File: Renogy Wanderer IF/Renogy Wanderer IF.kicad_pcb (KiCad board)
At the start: 2 copper layers, 50.8 x 40.6 mm, 4 parts, among them J1 Conn_01x04, U1 WeMos_D1_mini

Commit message: Initial PCB design
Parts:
- removed A1: MINI-360, Module:MINI-360
- moved J1 28.3 mm to (99.1, 91.0), turned to 90 degrees
- moved U1 21.6 mm to (103.4, 52.1)
- moved A2 18.0 mm to (114.3, 86.4), turned to 180 degrees
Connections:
- J1 pad 1: +15V -> GND
- J1 pad 4: GND -> unconnected-(J1-Pad4)
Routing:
- net GND: track 0.00 -> 63.8 mm
- net +3V3: track 0.00 -> 38.1 mm
- net Net-(U1-Pad16): track 0.00 -> 34.1 mm, vias 0 -> 1
- net Net-(U1-Pad15): track 0.00 -> 28.4 mm, vias 0 -> 1
- net Net-(J1-Pad3): track 0.00 -> 11.2 mm, vias 0 -> 1
- net Net-(J1-Pad2): track 0.00 -> 10.8 mm, vias 0 -> 1
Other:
- board size 50.8 x 40.6 mm -> 35.6 x 50.8 mm
- board text added: "USB"

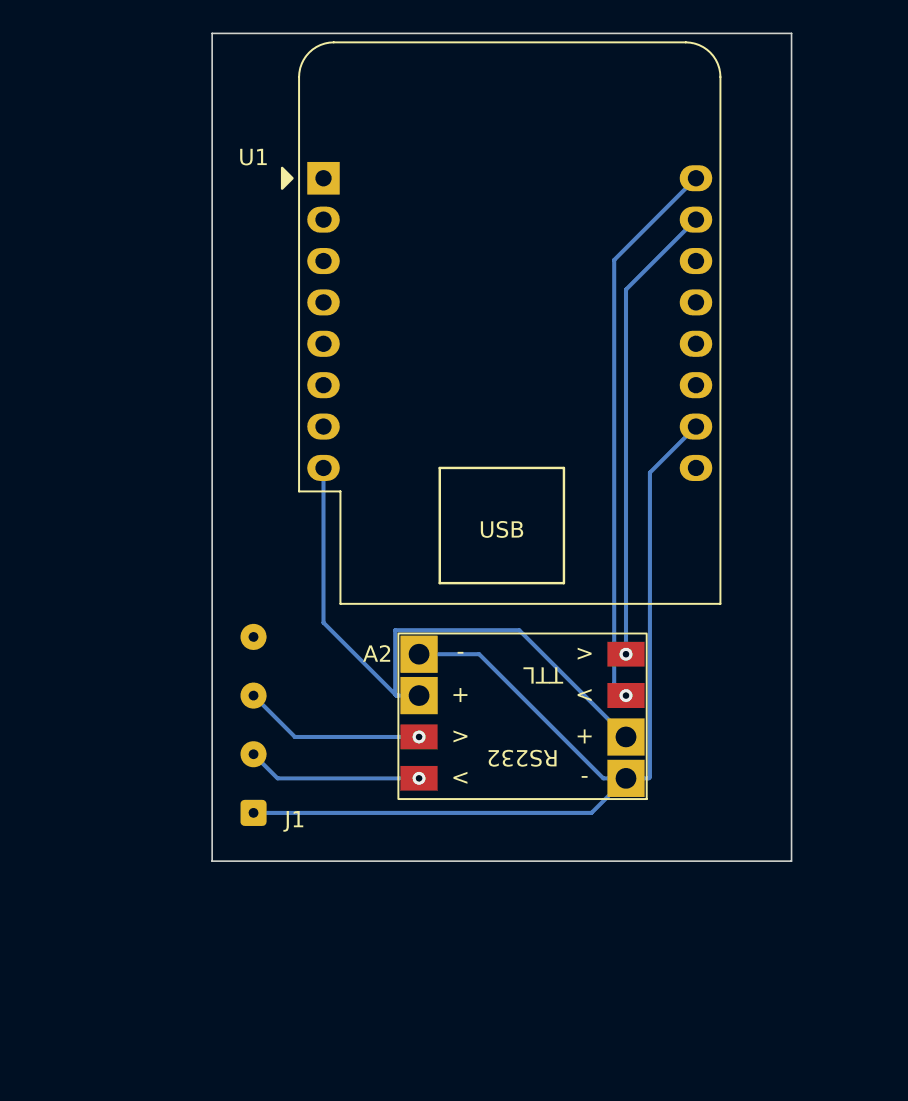
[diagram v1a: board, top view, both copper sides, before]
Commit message: Add wake from sleep
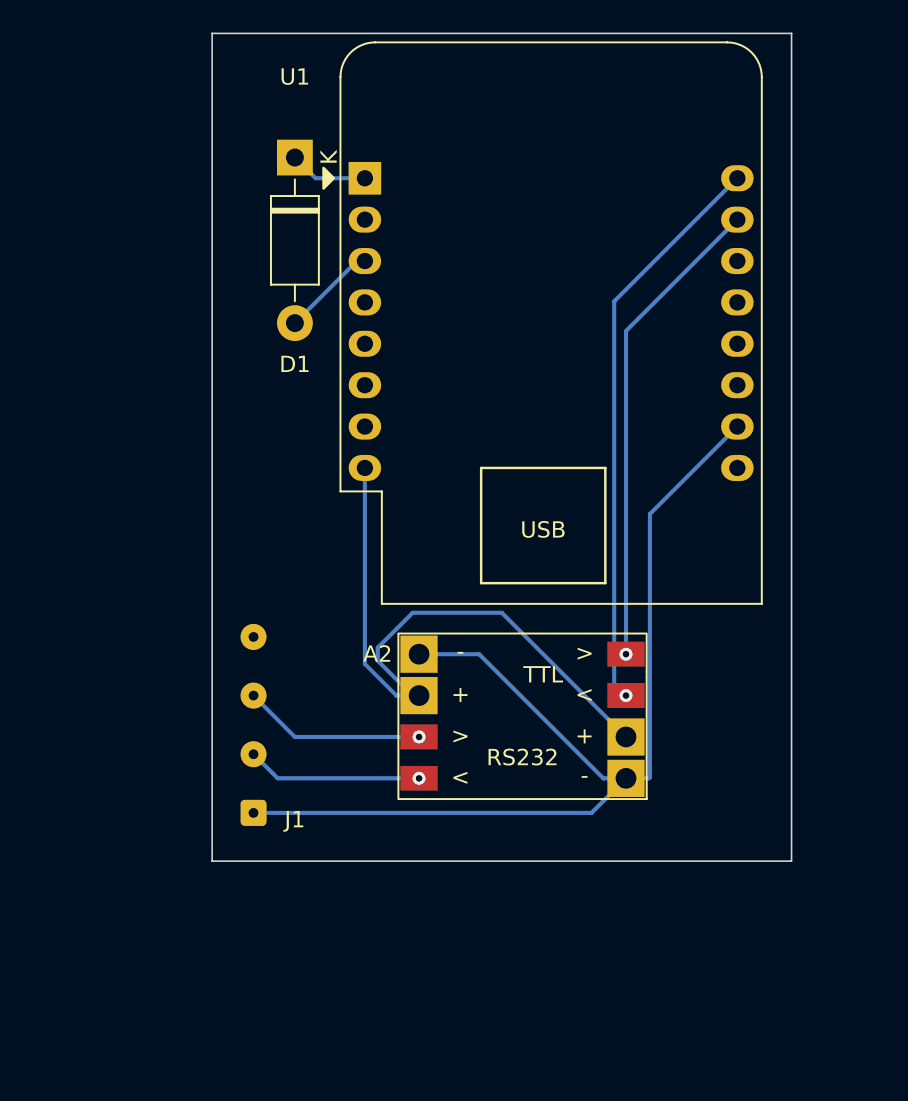
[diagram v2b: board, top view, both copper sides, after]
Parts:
- added D1: D_Schottky, Diode_THT:D_DO-41_SOD81_P10.16mm_Horizontal, F.Cu at (101.6, 50.8)
- moved U1 2.54 mm to (105.9, 52.1)
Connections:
- U1 pad 1: unconnected-(U1-Pad1) -> Net-(U1-Pad1)
- U1 pad 3: unconnected-(U1-Pad3) -> Net-(U1-Pad3)
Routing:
- net Net-(U1-Pad3): track 0.00 -> 5.87 mm
- net Net-(U1-Pad1): track 0.00 -> 4.82 mm
- net +3V3: track 38.1 -> 39.7 mm
- net GND: track 63.8 -> 64.8 mm
- net Net-(A2-Pad12): track 28.4 -> 29.5 mm
- net Net-(A2-Pad11): track 34.1 -> 35.2 mm

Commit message: Invert the RS232 module for easier mounting
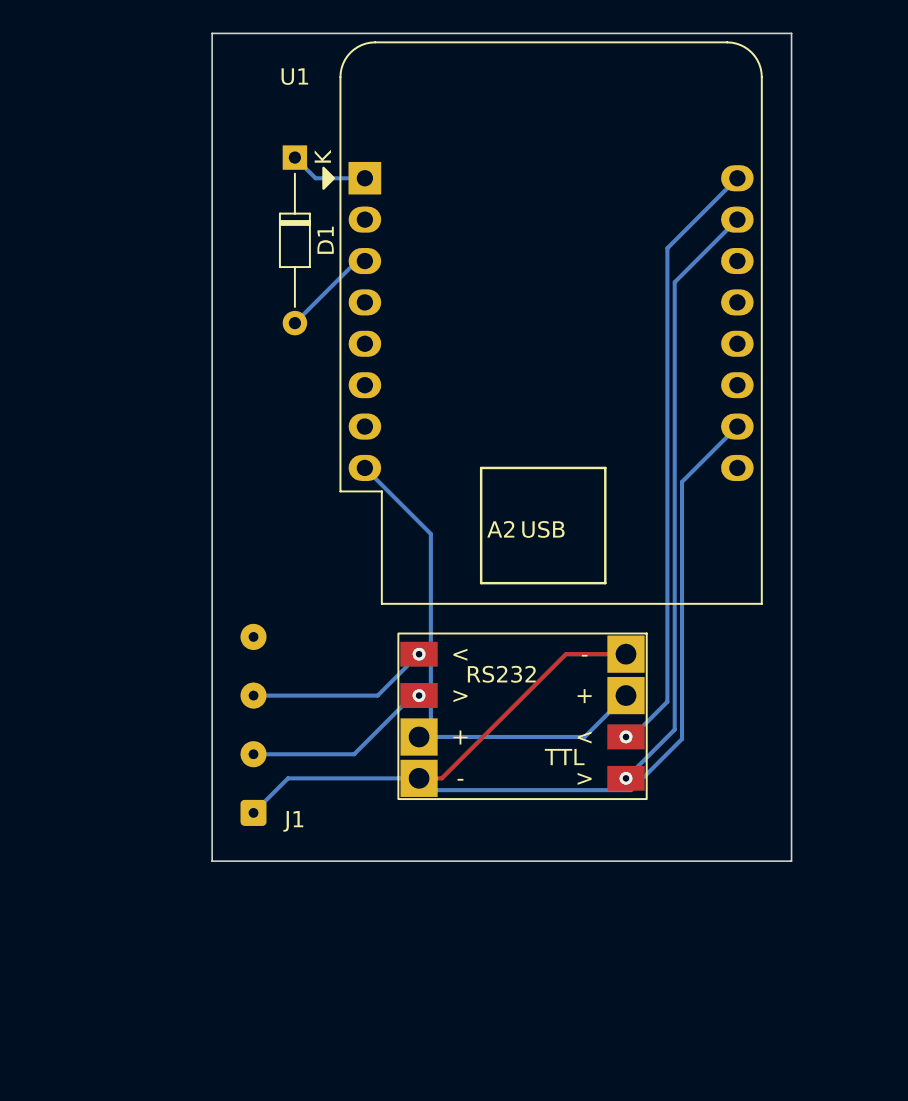
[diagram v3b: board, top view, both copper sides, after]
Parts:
- A2: footprint Module:MAX3232 module -> Module:MAX3232 module inverted
- D1: footprint Diode_THT:D_DO-41_SOD81_P10.16mm_Horizontal -> Diode_THT:D_DO-34_SOD68_P10.16mm_Horizontal
- moved A2 3.59 mm to (116.8, 83.8), turned to 0 degrees
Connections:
- J1 pad 2: Net-(A2-Pad14) -> Net-(A2-Pad13)
- J1 pad 3: Net-(A2-Pad13) -> Net-(A2-Pad14)
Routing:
- net Net-(A2-Pad12): track 29.5 -> 37.1 mm
- net +3V3: track 39.7 -> 32.2 mm
- net Net-(A2-Pad11): track 35.2 -> 37.3 mm
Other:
- board text added: "+ RX TX -"
